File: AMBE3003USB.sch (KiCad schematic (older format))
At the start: 95 parts, among them J1 McBSP, J2 CODEC_SPI_I2C, J3 ACONF, P1 CONN_02X16, P2 USB_B, U1 AMBE3003, U2 LD1117S33TR, U3 TPS3805, U4 FT232RL, U5 TPS78319, X1 TCXO3

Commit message: Re-organized Codec Connector
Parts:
- removed J2: CODEC_SPI_I2C, symbol CONN_02X06
- added J?: CODEC, symbol CONN_02X05
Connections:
- net labels added: I2C_CLK, I2C_DATA, SPI_CLK, SPI_FSn, SPI_RX_DATA, SPI_TX_DATA
- wire segments 357 -> 352
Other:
- moved on the sheet: C1, C10, C11, C12, C13, C14, C15, C16, C17, C18, C19, C2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

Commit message: Added footprints
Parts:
- removed P2: USB_B, symbol USB_B-RESCUE-AMBE3003USB
- removed X1: TCXO3, symbol TCXO3-RESCUE-AMBE3003USB
- added C31: 100n, Capacitors_SMD:C_0603_HandSoldering, symbol C
- added J4: USB_OTG, Connectors:USB_Mini-B, symbol USB_OTG
- added X?: SG-210STF, Oscillators:Oscillator_SMD_SeikoEpson_SG210-4pin_2.5x2.0mm, symbol SG-210STF
- C1, C2, C3: footprint (none) -> Capacitors_SMD:C_0603_HandSoldering
- C10: renamed from C19; footprint (none) -> Capacitors_SMD:C_0603_HandSoldering
- C11: renamed from C4; footprint (none) -> Capacitors_Tantalum_SMD:CP_Tantalum_Case-D_EIA-7343-31_Hand
- C12: renamed from C21; footprint (none) -> Capacitors_SMD:C_0603_HandSoldering
- C13: renamed from C23; footprint (none) -> Capacitors_SMD:C_0603_HandSoldering
- C14: renamed from C25; footprint (none) -> Capacitors_SMD:C_0603_HandSoldering
- C15: renamed from C5; footprint (none) -> Capacitors_SMD:C_0603_HandSoldering
- C16: renamed from C26; footprint (none) -> Capacitors_SMD:C_0603_HandSoldering
- C17: renamed from C6; footprint (none) -> Capacitors_Tantalum_SMD:CP_Tantalum_Case-D_EIA-7343-31_Hand
- C18: renamed from C27; footprint (none) -> Capacitors_SMD:C_0603_HandSoldering
- C19: renamed from C28; footprint (none) -> Capacitors_SMD:C_0603_HandSoldering
- C20: renamed from C7; footprint (none) -> Capacitors_SMD:C_0603_HandSoldering
- C21: renamed from C8; footprint (none) -> Capacitors_SMD:C_0603_HandSoldering
- C22: renamed from C30; footprint (none) -> Capacitors_SMD:C_0603_HandSoldering
- C23: renamed from C9; footprint (none) -> Capacitors_SMD:C_0603_HandSoldering
- C24: renamed from C13; footprint (none) -> Capacitors_SMD:C_0603_HandSoldering
- C25: renamed from C14; footprint (none) -> Capacitors_Tantalum_SMD:CP_Tantalum_Case-D_EIA-7343-31_Hand
- C26: renamed from C17; footprint (none) -> Capacitors_SMD:C_0603_HandSoldering
- C27: renamed from C20; footprint (none) -> Capacitors_Tantalum_SMD:CP_Tantalum_Case-D_EIA-7343-31_Hand
- C28: renamed from C22; footprint (none) -> Capacitors_Tantalum_SMD:CP_Tantalum_Case-D_EIA-7343-31_Hand
- C29: renamed from C24; footprint (none) -> Capacitors_SMD:C_0603_HandSoldering
- C30: renamed from C29; footprint (none) -> Capacitors_Tantalum_SMD:CP_Tantalum_Case-D_EIA-7343-31_Hand
- C4: renamed from C12; footprint (none) -> Capacitors_SMD:C_0603_HandSoldering
- C5: renamed from C15; footprint (none) -> Capacitors_SMD:C_0603_HandSoldering
- C6: renamed from C16; footprint (none) -> Capacitors_SMD:C_0603_HandSoldering
- C7: renamed from C10; footprint (none) -> Capacitors_SMD:C_0603_HandSoldering
- C8: renamed from C18; footprint (none) -> Capacitors_SMD:C_0603_HandSoldering
- C9: renamed from C11; footprint (none) -> Capacitors_Tantalum_SMD:CP_Tantalum_Case-D_EIA-7343-31_Hand
- D1, D2, D3: footprint (none) -> LEDs:LED_0603
- J1: footprint (none) -> Pin_Headers:Pin_Header_Straight_2x04_Pitch2.54mm
- J2: renamed from J3; footprint (none) -> Pin_Headers:Pin_Header_Straight_2x03_Pitch2.54mm
- J3: renamed from J?; footprint (none) -> Pin_Headers:Pin_Header_Straight_2x05_Pitch2.54mm
- L1: footprint (none) -> Inductors_SMD:L_0603_HandSoldering
- P1: footprint (none) -> Pin_Headers:Pin_Header_Straight_2x16_Pitch2.54mm
- R1, R10, R11, R12, R13, R14, R15, R16, R17, R18, R2, R3, R38, R39, R4, R40, R41, R42, R43, R44, R45, R46, R47, R5, R6, R7, R8, R9: footprint (none) -> Resistors_SMD:R_0603_HandSoldering
- R19: renamed from R37; footprint (none) -> Resistors_SMD:R_0603_HandSoldering
- R20: renamed from R19; footprint (none) -> Resistors_SMD:R_0603_HandSoldering
- R21: renamed from R20; footprint (none) -> Resistors_SMD:R_0603_HandSoldering
- R22: renamed from R21; footprint (none) -> Resistors_SMD:R_0603_HandSoldering
- R23: renamed from R22; footprint (none) -> Resistors_SMD:R_0603_HandSoldering
- R24: renamed from R23; footprint (none) -> Resistors_SMD:R_0603_HandSoldering
- R25: renamed from R24; footprint (none) -> Resistors_SMD:R_0603_HandSoldering
- R26: renamed from R25; footprint (none) -> Resistors_SMD:R_0603_HandSoldering
- R27: renamed from R26; footprint (none) -> Resistors_SMD:R_0603_HandSoldering
- R28: renamed from R27; footprint (none) -> Resistors_SMD:R_0603_HandSoldering
- R29: renamed from R28; footprint (none) -> Resistors_SMD:R_0603_HandSoldering
- R30: renamed from R29; footprint (none) -> Resistors_SMD:R_0603_HandSoldering
- R31: renamed from R30; footprint (none) -> Resistors_SMD:R_0603_HandSoldering
- R32: renamed from R31; footprint (none) -> Resistors_SMD:R_0603_HandSoldering
- R33: renamed from R32; footprint (none) -> Resistors_SMD:R_0603_HandSoldering
- R34: renamed from R33; footprint (none) -> Resistors_SMD:R_0603_HandSoldering
- R35: renamed from R34; footprint (none) -> Resistors_SMD:R_0603_HandSoldering
- R36: renamed from R35; footprint (none) -> Resistors_SMD:R_0603_HandSoldering
- R37: renamed from R36; footprint (none) -> Resistors_SMD:R_0603_HandSoldering
- TP1, TP2, TP3: footprint (none) -> Measurement_Points:Measurement_Point_Round-SMD-Pad_Big
- U1: footprint (none) -> Housings_QFP:LQFP-128_14x14mm_Pitch0.4mm
- U2: footprint TO_SOT_Packages_SMD:SOT-223 -> TO_SOT_Packages_SMD:SOT-223-3Lead_TabPin2
- U3: footprint (none) -> TI:DCK
- U4: footprint SSOP-28 -> Housings_SSOP:SSOP-28_5.3x10.2mm_Pitch0.65mm
- U5: footprint (none) -> TO_SOT_Packages_SMD:SOT-23-5_HandSoldering
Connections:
- wire segments 352 -> 360
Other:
- moved on the sheet: C15, C20, C25, L1

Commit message: Align capacitor values
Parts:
- C11, C17, C2, C3: value 10u -> 10µ
- J4: symbol USB_OTG -> USB_OTG-RESCUE-AMBE3003USB
- gave numbers to parts that had none: 1
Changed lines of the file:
@@
 P 1000 6750
 F 0 "C3" H 1025 6850 50  0000 L CNN
-F 1 "10u" H 1025 6650 50  0000 L CNN
+F 1 "10µ" H 1025 6650 50  0000 L CNN
 F 2 "Capacitors_SMD:C_0603_HandSoldering" H 1038 6600 50  0001 C CNN
 F 3 "" H 1000 6750 50  0000 C CNN
@@
 P 750 6750
 F 0 "C2" H 775 6850 50  0000 L CNN
-F 1 "10u" H 775 6650 50  0000 L CNN
+F 1 "10µ" H 775 6650 50  0000 L CNN
 F 2 "Capacitors_SMD:C_0603_HandSoldering" H 788 6600 50  0001 C CNN
 F 3 "" H 750 6750 50  0000 C CNN
@@
 P 5800 1350
 F 0 "C11" H 5825 1450 50  0000 L CNN
-F 1 "10u" H 5825 1250 50  0000 L CNN
+F 1 "10µ" H 5825 1250 50  0000 L CNN
 F 2 "Capacitors_Tantalum_SMD:CP_Tantalum_Case-D_EIA-7343-31_Hand" H 5838 1200 50  0001 C CNN
 F 3 "" H 5800 1350 50  0000 C CNN
@@
 P 6800 1350
 F 0 "C17" H 6825 1450 50  0000 L CNN
-F 1 "10u" H 6825 1250 50  0000 L CNN
+F 1 "10µ" H 6825 1250 50  0000 L CNN
 F 2 "Capacitors_Tantalum_SMD:CP_Tantalum_Case-D_EIA-7343-31_Hand" H 6838 1200 50  0001 C CNN
 F 3 "" H 6800 1350 50  0000 C CNN
@@
 $EndComp
 $Comp
-L GND #PWR25
+L GND #PWR27
 U 1 1 59299142
 P 6300 1600
-F 0 "#PWR25" H 6300 1350 50  0001 C CNN
+F 0 "#PWR27" H 6300 1350 50  0001 C CNN
 F 1 "GND" H 6300 1450 50  0000 C CNN
 F 2 "" H 6300 1600 50  0000 C CNN
@@
 SPI_FSn
 $Comp
-L USB_OTG J4
+L USB_OTG-RESCUE-AMBE3003USB J4
 U 1 1 592902DE
 P 6550 3600
@@
 $EndComp
 $Comp
-L +1V9 #PWR26
+L +1V9 #PWR25
 U 1 1 591DCA69
 P 6050 6750
-F 0 "#PWR26" H 6050 6600 50  0001 C CNN
+F 0 "#PWR25" H 6050 6600 50  0001 C CNN
 F 1 "+1V9" H 6050 6890 50  0000 C CNN
 F 2 "" H 6050 6750 50  0000 C CNN
@@
 $EndComp
 $Comp
-L SG-210STF X?
+L SG-210STF X1
 U 1 1 592A4AE5
 P 6050 7150
-F 0 "X?" H 5850 7400 50  0000 L CNN
+F 0 "X1" H 5850 7400 50  0000 L CNN
 F 1 "SG-210STF" H 6100 6900 50  0000 L CNN
 F 2 "Oscillators:Oscillator_SMD_SeikoEpson_SG210-4pin_2.5x2.0mm" H 6500 6800 50  0001 C CNN
@@
 NoConn ~ 6350 7150
 $Comp
-L GND #PWR?
+L GND #PWR26
 U 1 1 592A5B6C
 P 6050 7550
-F 0 "#PWR?" H 6050 7300 50  0001 C CNN
+F 0 "#PWR26" H 6050 7300 50  0001 C CNN
 F 1 "GND" H 6050 7400 50  0000 C CNN
 F 2 "" H 6050 7550 50  0000 C CNN

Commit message: Change Cap footprint to case A
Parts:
- C11, C17, C25, C27, C28, C30, C9: footprint Capacitors_Tantalum_SMD:CP_Tantalum_Case-D_EIA-7343-31_Hand -> Capacitors_Tantalum_SMD:TantalC_SizeA_EIA-3216_HandSoldering

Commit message: Component Placement Done
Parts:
- TP1, TP2, TP3: footprint Measurement_Points:Measurement_Point_Round-SMD-Pad_Big -> Measurement_Points:Measurement_Point_Round-SMD-Pad_Small
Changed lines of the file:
@@
 F 0 "TP3" H 4300 3650 50  0000 C BNN
 F 1 "TEST" H 4300 3600 50  0000 C CNN
-F 2 "Measurement_Points:Measurement_Point_Round-SMD-Pad_Big" H 4300 3350 50  0001 C CNN
+F 2 "Measurement_Points:Measurement_Point_Round-SMD-Pad_Small" H 4300 3350 50  0001 C CNN
 F 3 "" H 4300 3350 50  0001 C CNN
 	1    4300 3350
@@
 F 0 "TP2" H 4100 3650 50  0000 C BNN
 F 1 "TEST" H 4100 3600 50  0000 C CNN
-F 2 "Measurement_Points:Measurement_Point_Round-SMD-Pad_Big" H 4100 3350 50  0001 C CNN
+F 2 "Measurement_Points:Measurement_Point_Round-SMD-Pad_Small" H 4100 3350 50  0001 C CNN
 F 3 "" H 4100 3350 50  0001 C CNN
 	1    4100 3350
@@
 F 0 "TP1" H 3900 3650 50  0000 C BNN
 F 1 "TEST" H 3900 3600 50  0000 C CNN
-F 2 "Measurement_Points:Measurement_Point_Round-SMD-Pad_Big" H 3900 3350 50  0001 C CNN
+F 2 "Measurement_Points:Measurement_Point_Round-SMD-Pad_Small" H 3900 3350 50  0001 C CNN
 F 3 "" H 3900 3350 50  0001 C CNN
 	1    3900 3350

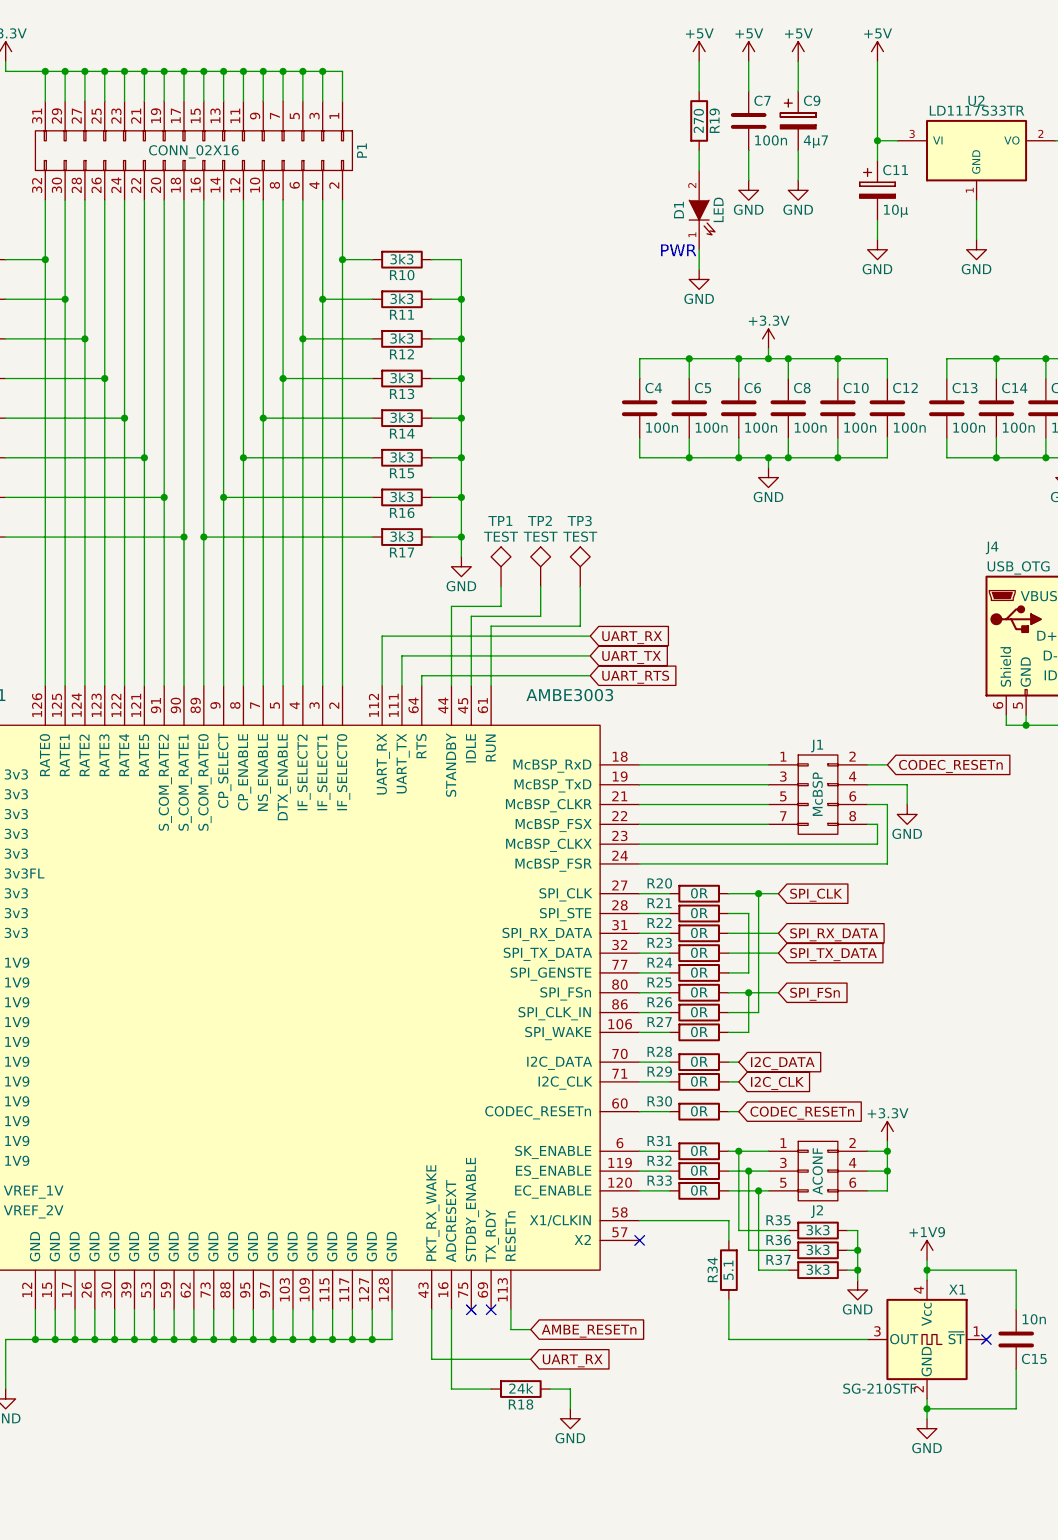
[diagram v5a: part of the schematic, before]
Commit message: Rounded corners, added descriptors
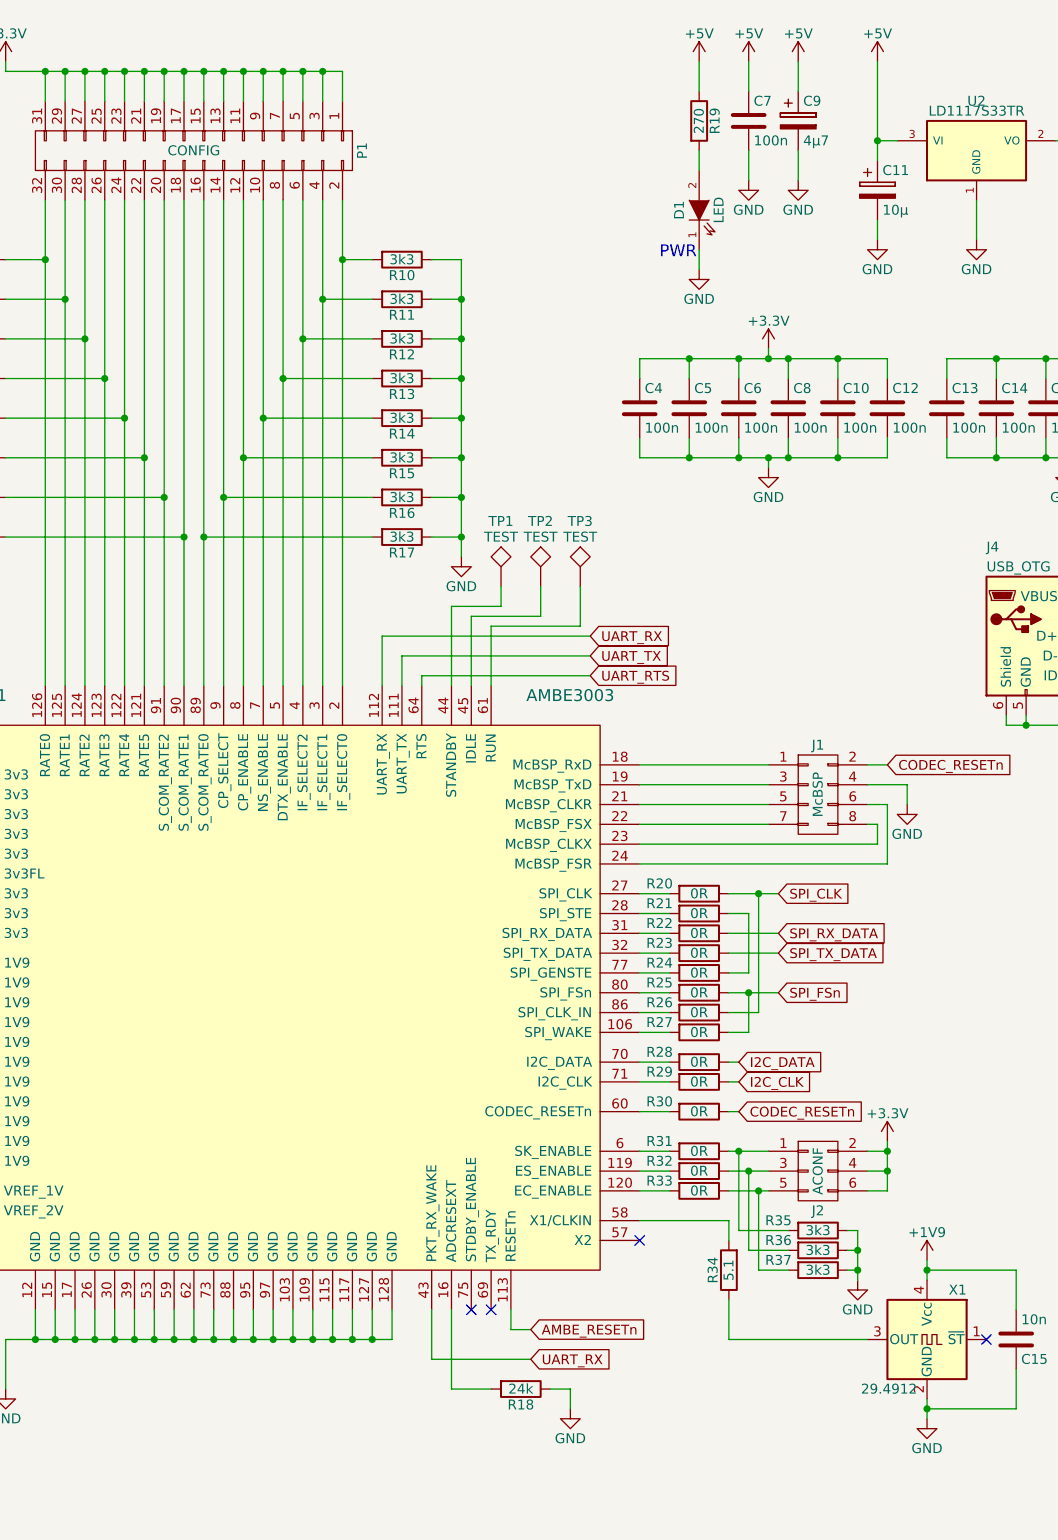
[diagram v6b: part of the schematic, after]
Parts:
- P1: value CONN_02X16 -> CONFIG
- X1: value SG-210STF -> 29.4912
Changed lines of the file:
@@
 P 2350 1150
 F 0 "P1" H 2350 2000 50  0000 C CNN
-F 1 "CONN_02X16" V 2350 1150 50  0000 C CNN
+F 1 "CONFIG" V 2350 1150 50  0000 C CNN
 F 2 "Pin_Headers:Pin_Header_Straight_2x16_Pitch2.54mm" H 2350 50  50  0001 C CNN
 F 3 "" H 2350 50  50  0000 C CNN
@@
 P 6050 7150
 F 0 "X1" H 5850 7400 50  0000 L CNN
-F 1 "SG-210STF" H 6100 6900 50  0000 L CNN
+F 1 "29.4912" H 6100 6900 50  0000 L CNN
 F 2 "Oscillators:Oscillator_SMD_SeikoEpson_SG210-4pin_2.5x2.0mm" H 6500 6800 50  0001 C CNN
 F 3 "" H 5950 7150 50  0001 C CNN
